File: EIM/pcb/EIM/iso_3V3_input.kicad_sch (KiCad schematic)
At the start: 7 parts, among them IC3 ILD213T

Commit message: added Arjun's comments, assigned some MCU pins
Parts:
- removed D7, D8: SMBJ5.0A, Diode_SMD:D_SMB, symbol Diode:SM6T10A
- removed IC3: ILD213T, SamacSys_Parts:SOIC127P610X350-8N, symbol SamacSys_Parts:ILD213T
- removed R15, R16: 220R, Resistor_SMD:R_0805_2012Metric_Pad1.20x1.40mm_HandSolder, symbol Device:R
- removed R17, R18: 10k, Resistor_SMD:R_0805_2012Metric_Pad1.20x1.40mm_HandSolder, symbol Device:R
- added D15, D16: SMBJ5.0A, Diode_SMD:D_SMB, symbol Diode:SM6T10A
- added IC4: ILD213T, SamacSys_Parts:SOIC127P610X350-8N, symbol SamacSys_Parts:ILD213T
- added R48, R49: 220R, Resistor_SMD:R_0805_2012Metric_Pad1.20x1.40mm_HandSolder, symbol Device:R
- added R50, R51: 10k, Resistor_SMD:R_0805_2012Metric_Pad1.20x1.40mm_HandSolder, symbol Device:R
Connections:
- net +3V3: now also R50.2, R51.2
- net A_IN+: now also R48.1
- net A_IN-: now also D15.2 (A2), IC4.2 (CATHODE_1)
- net A_OUT: now also IC4.8 (COLLECTOR_2), R50.1
- net B_IN+: now also R49.1
- net B_IN-: now also D16.2 (A2), IC4.4 (CATHODE_2)
- net B_OUT: now also IC4.6 (COLLECTOR), R51.1
- net GND: now also IC4.5 (EMITTER), IC4.7 (EMITTER_2)
- new net: D16.1 (A1), IC4.3 (ANODE_2), R49.2
- new net: D15.1 (A1), IC4.1 (ANODE_1), R48.2
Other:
- note added: "opto timing info with 10 mA through LED turn-on time = 3 us turn-off time = 10 us quickest cycle = 15 us (2 us arbitrary plateau time) --> 66 kHz max frequency"

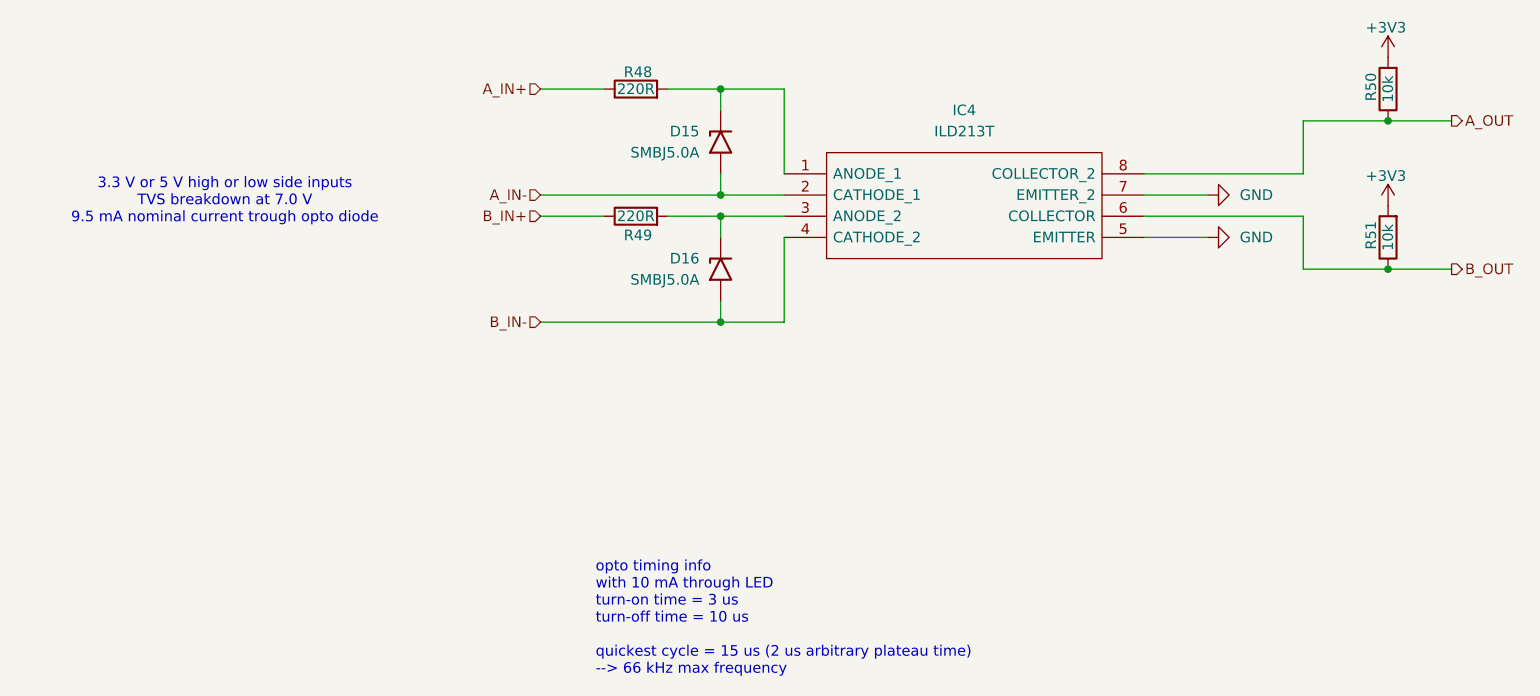
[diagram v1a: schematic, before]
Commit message: Layout 75% done, before 8V bus deletion
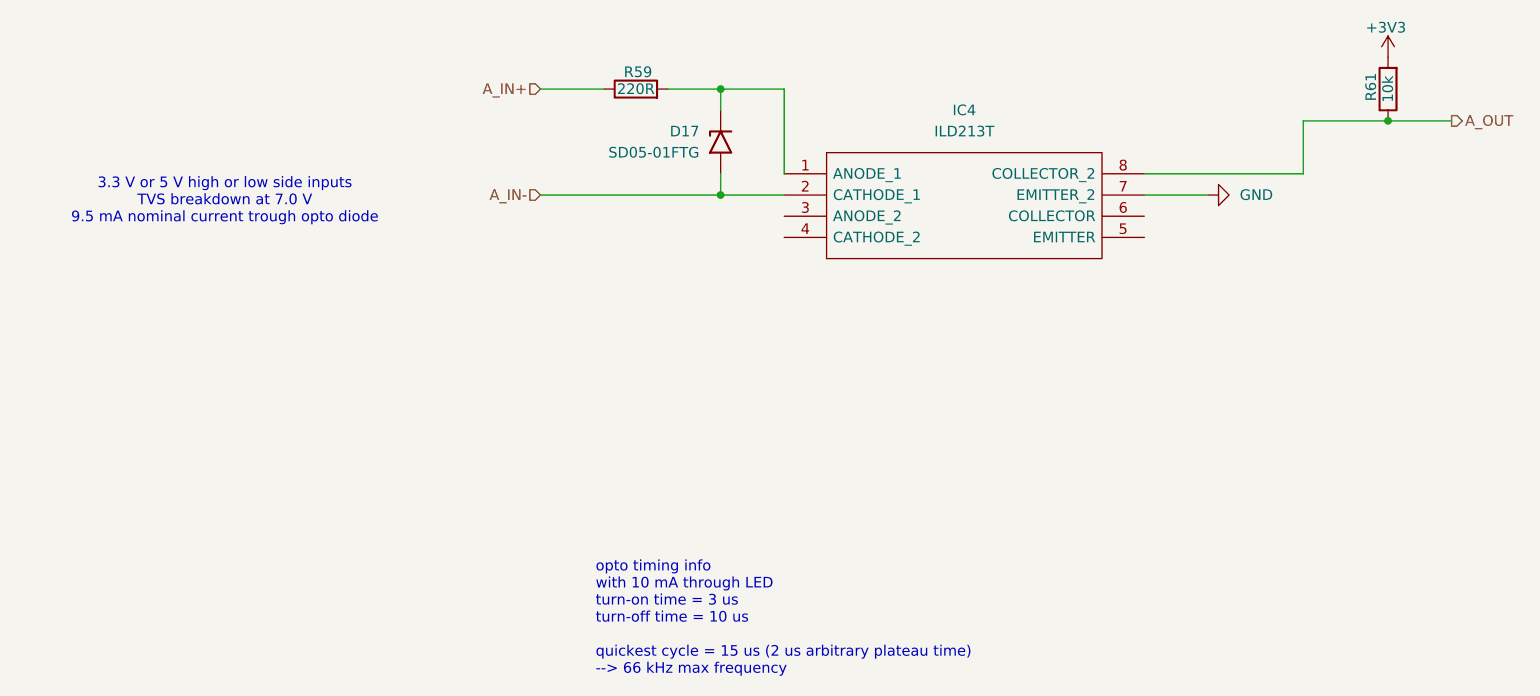
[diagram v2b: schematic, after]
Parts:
- removed D16: SMBJ5.0A, Diode_SMD:D_SMB, symbol Diode:SM6T10A
- removed R49: 220R, Resistor_SMD:R_0805_2012Metric_Pad1.20x1.40mm_HandSolder, symbol Device:R
- removed R51: 10k, Resistor_SMD:R_0805_2012Metric_Pad1.20x1.40mm_HandSolder, symbol Device:R
- D17: renamed from D15; value SMBJ5.0A -> SD05-01FTG; footprint Diode_SMD:D_SMB -> Diode_SMD:D_SOD-323
- renumbered R48 to R59, R50 to R61
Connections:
- net GND: no longer IC4.5 (EMITTER)
- net B_IN-: no longer names the net of IC4.4 (CATHODE_2)
- net B_OUT: no longer names the net of IC4.6 (COLLECTOR)

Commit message: All components placed and pins assigned.
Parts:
- renumbered D17 to D15, R59 to R54, R61 to R55
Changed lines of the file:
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@@
 		(dnp no)
 		(fields_autoplaced yes)
-		(property "Reference" "#PWR0125"
+		(property "Reference" "#PWR0118"
 			(at 180.34 93.98 0)
 			(effects
@@
 			(project "EIM"
 				(path "/2e0b3b3d-5537-41dc-9fad-4fb33afdbfad/3529c61d-b0aa-4683-a953-a419c39aa299"
-					(reference "#PWR0125")
+					(reference "#PWR0118")
 					(unit 1)
 				)
@@
 		(on_board yes)
 		(dnp no)
-		(property "Reference" "R61"
+		(property "Reference" "R55"
 			(at 193.548 81.026 90)
 			(effects
@@
 			(project "EIM"
 				(path "/2e0b3b3d-5537-41dc-9fad-4fb33afdbfad/3529c61d-b0aa-4683-a953-a419c39aa299"
-					(reference "R61")
+					(reference "R55")
 					(unit 1)
 				)
@@
 		(on_board yes)
 		(dnp no)
-		(property "Reference" "D17"
+		(property "Reference" "D15"
 			(at 113.03 86.3599 90)
 			(effects
@@
 			(project "EIM"
 				(path "/2e0b3b3d-5537-41dc-9fad-4fb33afdbfad/3529c61d-b0aa-4683-a953-a419c39aa299"
-					(reference "D17")
+					(reference "D15")
 					(unit 1)
 				)
@@
 		(on_board yes)
 		(dnp no)
-		(property "Reference" "R59"
+		(property "Reference" "R54"
 			(at 105.664 79.248 90)
 			(effects
@@
 			(project "EIM"
 				(path "/2e0b3b3d-5537-41dc-9fad-4fb33afdbfad/3529c61d-b0aa-4683-a953-a419c39aa299"
-					(reference "R59")
+					(reference "R54")
 					(unit 1)
 				)
@@
 		(on_board yes)
 		(dnp no)
-		(property "Reference" "#PWR0127"
+		(property "Reference" "#PWR0119"
 			(at 195.58 81.28 0)
 			(effects
@@
 			(project "EIM"
 				(path "/2e0b3b3d-5537-41dc-9fad-4fb33afdbfad/3529c61d-b0aa-4683-a953-a419c39aa299"
-					(reference "#PWR0127")
-					(unit 1)
-				)
+					(reference "#PWR0119")
+					(unit 1)
+				)
